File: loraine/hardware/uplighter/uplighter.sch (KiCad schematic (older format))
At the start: 10 parts, among them K1 CONN_3, K2 CONN_3, K3 CONN_3, U1 TL4242, U2 TL4242, U3 TL4242

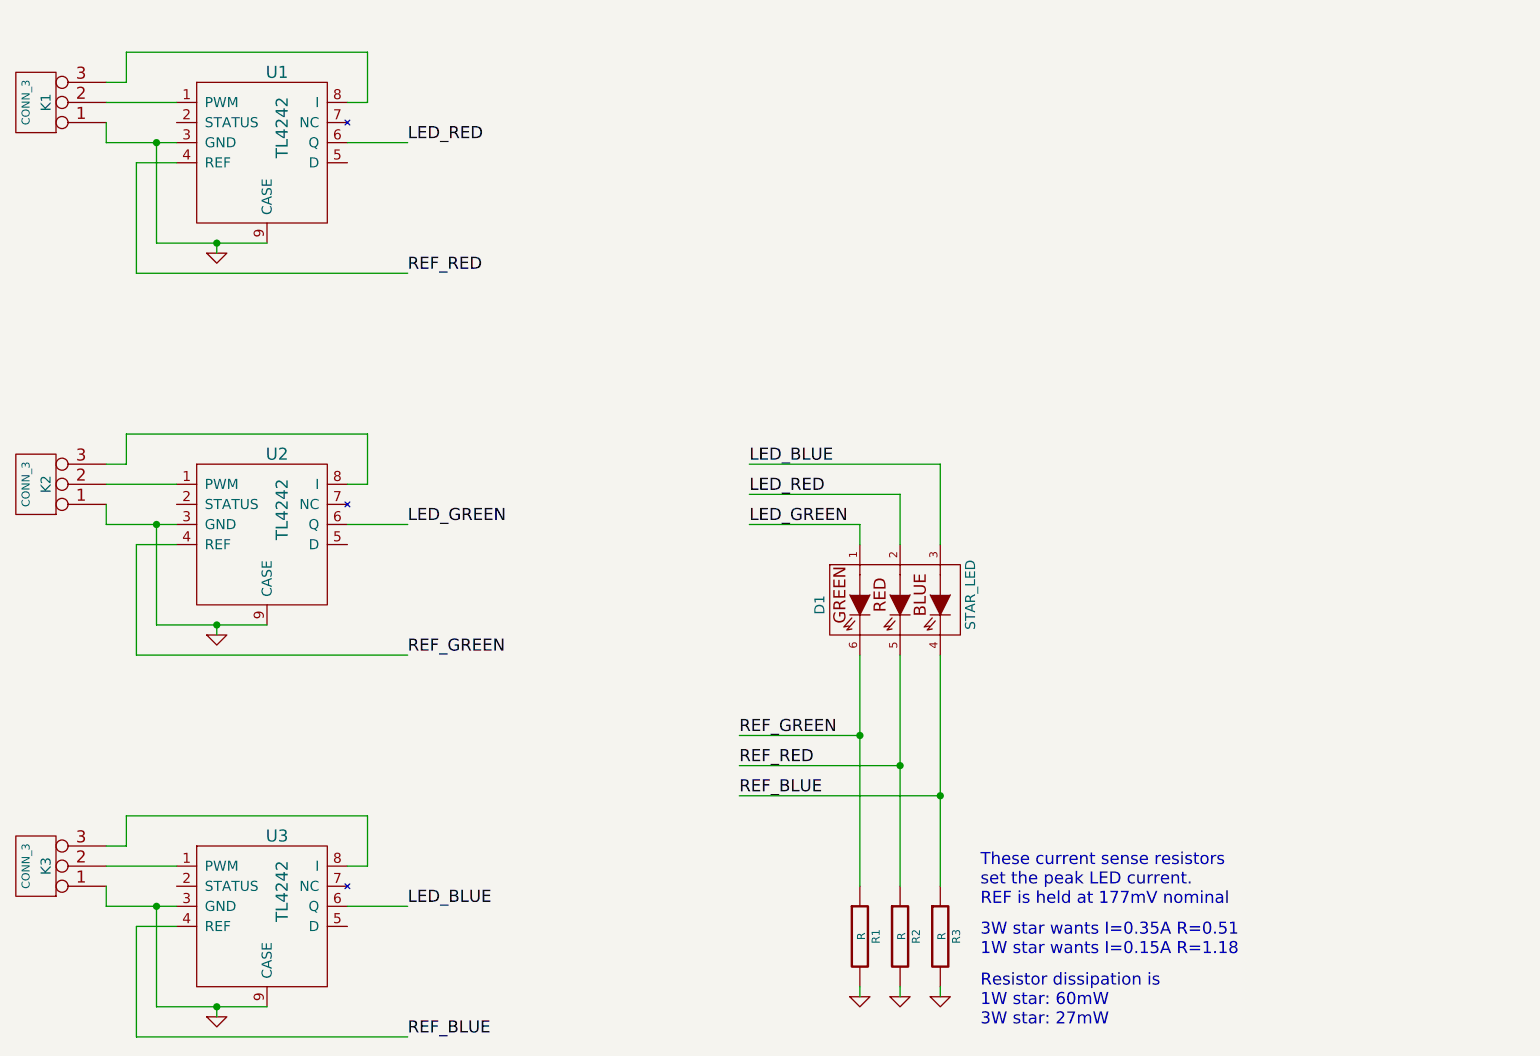
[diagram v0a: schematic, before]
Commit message: Proposed output driver for node h/w
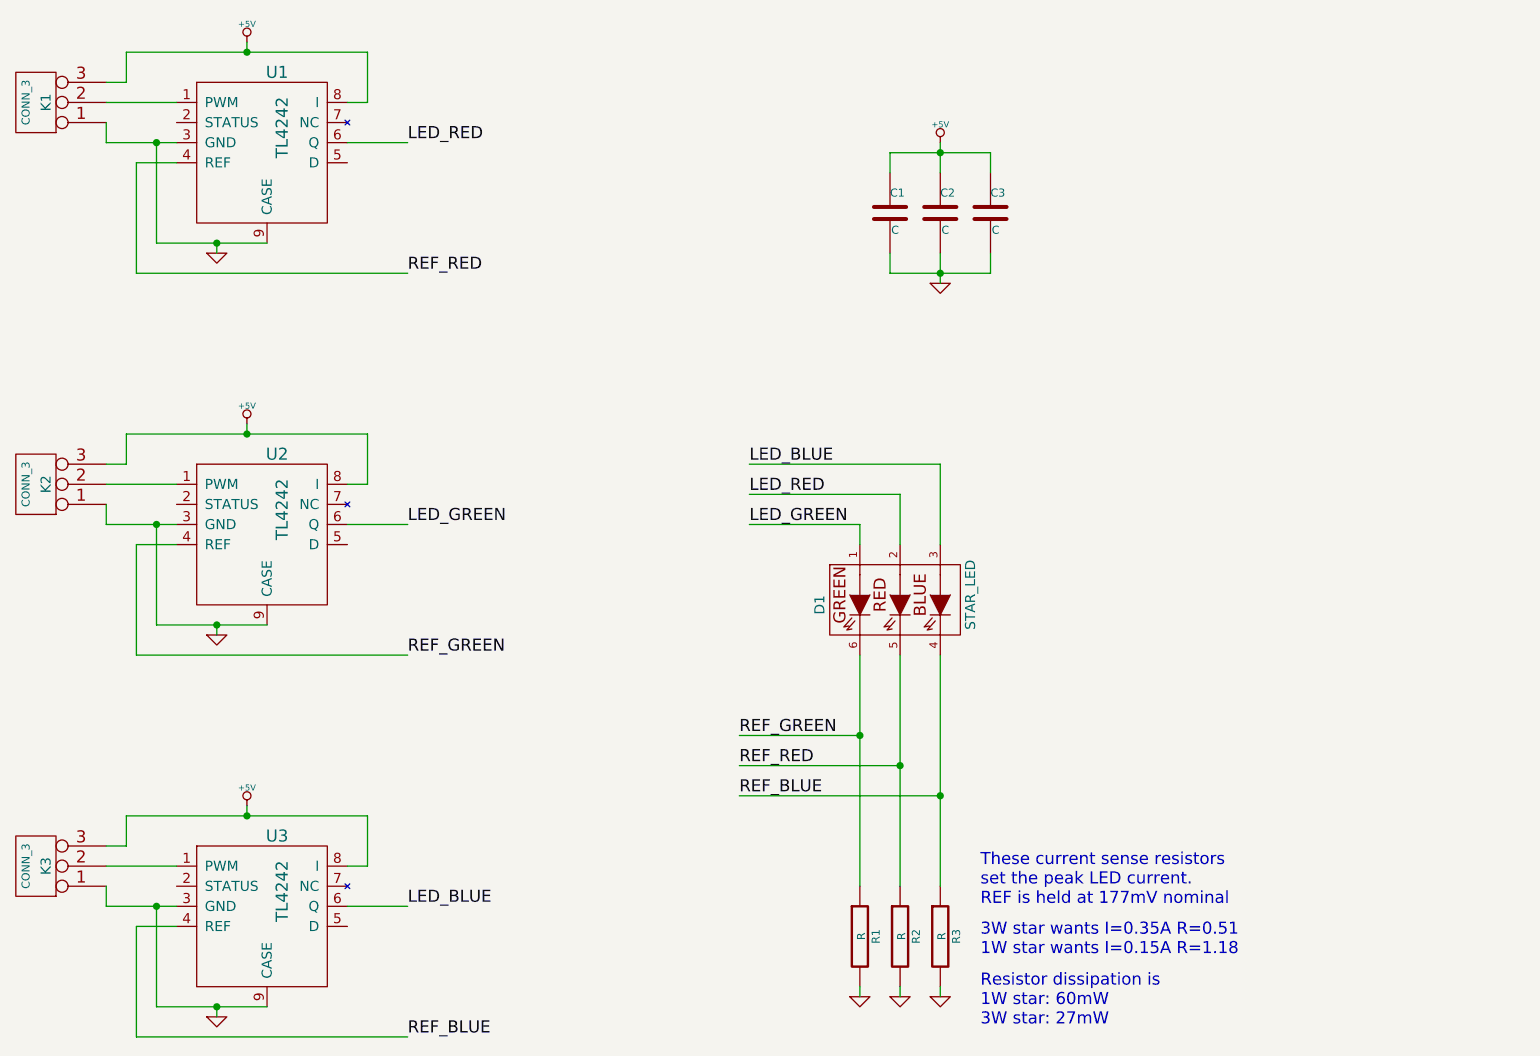
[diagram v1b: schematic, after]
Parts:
- added C1, C2, C3: C, symbol C
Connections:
- net GND: now also C1.2, C2.2, C3.2
- net +5V: now reaches K1.3 (P3), U1.8 (I)
- net +5V: now also K2.3 (P3), K3.3 (P3), U2.8 (I), U3.8 (I), C1.1, C2.1, C3.1
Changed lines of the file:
@@
 	1    0    0    -1
 $EndComp
-Wire Wire Line
-	3150 1650 3450 1650
-Wire Wire Line
-	1950 1650 2300 1650
-Wire Wire Line
-	2200 2150 2750 2150
-Wire Wire Line
-	2200 1650 2200 2150
-Wire Wire Line
-	2300 1750 2100 1750
-Wire Wire Line
-	1950 1450 2300 1450
-Wire Wire Line
-	1950 1350 2050 1350
-Wire Wire Line
-	2050 1350 2050 1200
-Wire Wire Line
-	2050 1200 3250 1200
-Wire Wire Line
-	3250 1200 3250 1450
-Wire Wire Line
-	3250 1450 3150 1450
-Wire Wire Line
-	1950 1550 1950 1650
-Connection ~ 2200 1650
-Wire Wire Line
-	2100 1750 2100 2300
-Wire Wire Line
-	2100 2300 3450 2300
-Wire Wire Line
-	3150 3550 3450 3550
-Wire Wire Line
-	1950 3550 2300 3550
-Wire Wire Line
-	2200 4050 2750 4050
-Wire Wire Line
-	2200 3550 2200 4050
-Wire Wire Line
-	2300 3650 2100 3650
-Wire Wire Line
-	1950 3350 2300 3350
-Wire Wire Line
-	1950 3250 2050 3250
-Wire Wire Line
-	2050 3250 2050 3100
-Wire Wire Line
-	2050 3100 3250 3100
-Wire Wire Line
-	3250 3100 3250 3350
-Wire Wire Line
-	3250 3350 3150 3350
-Wire Wire Line
-	1950 3450 1950 3550
-Connection ~ 2200 3550
-Wire Wire Line
-	2100 3650 2100 4200
-Wire Wire Line
-	2100 4200 3450 4200
-Wire Wire Line
-	3150 5450 3450 5450
-Wire Wire Line
-	1950 5450 2300 5450
-Wire Wire Line
-	2200 5950 2750 5950
-Wire Wire Line
-	2200 5450 2200 5950
-Wire Wire Line
-	2300 5550 2100 5550
-Wire Wire Line
-	1950 5250 2300 5250
-Wire Wire Line
-	1950 5150 2050 5150
-Wire Wire Line
-	2050 5150 2050 5000
-Wire Wire Line
-	2050 5000 3250 5000
-Wire Wire Line
-	3250 5000 3250 5250
-Wire Wire Line
-	3250 5250 3150 5250
-Wire Wire Line
-	1950 5350 1950 5450
-Connection ~ 2200 5450
-Wire Wire Line
-	2100 5550 2100 6100
-Wire Wire Line
-	2100 6100 3450 6100
-Wire Wire Line
-	5700 4200 5700 5350
-Wire Wire Line
-	5900 4200 5900 5350
-Wire Wire Line
-	6100 4200 6100 5350
-Wire Wire Line
-	6100 5850 6100 5900
-Wire Wire Line
-	5900 5900 5900 5850
-Wire Wire Line
-	5700 5850 5700 5900
-Wire Wire Line
-	2500 2200 2500 2150
-Connection ~ 2500 2150
 $Comp
 L GND #PWR05
@@
 	1    0    0    -1
 $EndComp
-Wire Wire Line
-	2500 4100 2500 4050
-Connection ~ 2500 4050
 $Comp
 L GND #PWR06
@@
 	1    0    0    -1
 $EndComp
-Wire Wire Line
-	2500 6000 2500 5950
-Connection ~ 2500 5950
 Text Label 5150 3550 0    60   ~ 0
 LED_GREEN
@@
 Text Label 5150 3250 0    60   ~ 0
 LED_BLUE
-Wire Wire Line
-	5150 3250 6100 3250
-Wire Wire Line
-	6100 3250 6100 3650
-Wire Wire Line
-	5150 3400 5900 3400
-Wire Wire Line
-	5900 3400 5900 3650
-Wire Wire Line
-	5150 3550 5700 3550
-Wire Wire Line
-	5700 3550 5700 3650
 Text Label 5100 4600 0    60   ~ 0
 REF_GREEN
@@
 Text Label 5100 4750 0    60   ~ 0
 REF_RED
+$Comp
+L +5V #PWR07
+U 1 1 537A665B
+P 2650 1150
+F 0 "#PWR07" H 2650 1240 20  0001 C CNN
+F 1 "+5V" H 2650 1240 30  0000 C CNN
+F 2 "" H 2650 1150 60  0000 C CNN
+F 3 "" H 2650 1150 60  0000 C CNN
+	1    2650 1150
+	1    0    0    -1
+$EndComp
+$Comp
+L +5V #PWR08
+U 1 1 537A6711
+P 2650 3050
+F 0 "#PWR08" H 2650 3140 20  0001 C CNN
+F 1 "+5V" H 2650 3140 30  0000 C CNN
+F 2 "" H 2650 3050 60  0000 C CNN
+F 3 "" H 2650 3050 60  0000 C CNN
+	1    2650 3050
+	1    0    0    -1
+$EndComp
+$Comp
+L +5V #PWR09
+U 1 1 537A67B5
+P 2650 4950
+F 0 "#PWR09" H 2650 5040 20  0001 C CNN
+F 1 "+5V" H 2650 5040 30  0000 C CNN
+F 2 "" H 2650 4950 60  0000 C CNN
+F 3 "" H 2650 4950 60  0000 C CNN
+	1    2650 4950
+	1    0    0    -1
+$EndComp
+$Comp
+L +5V #PWR010
+U 1 1 537A6897
+P 6100 1650
+F 0 "#PWR010" H 6100 1740 20  0001 C CNN
+F 1 "+5V" H 6100 1740 30  0000 C CNN
+F 2 "" H 6100 1650 60  0000 C CNN
+F 3 "" H 6100 1650 60  0000 C CNN
+	1    6100 1650
+	1    0    0    -1
+$EndComp
+$Comp
+L C C1
+U 1 1 537A69DC
+P 5850 2000
+F 0 "C1" H 5850 2100 40  0000 L CNN
+F 1 "C" H 5856 1915 40  0000 L CNN
+F 2 "" H 5888 1850 30  0000 C CNN
+F 3 "" H 5850 2000 60  0000 C CNN
+	1    5850 2000
+	1    0    0    -1
+$EndComp
+$Comp
+L C C2
+U 1 1 537A6A0C
+P 6100 2000
+F 0 "C2" H 6100 2100 40  0000 L CNN
+F 1 "C" H 6106 1915 40  0000 L CNN
+F 2 "" H 6138 1850 30  0000 C CNN
+F 3 "" H 6100 2000 60  0000 C CNN
+	1    6100 2000
+	1    0    0    -1
+$EndComp
+$Comp
+L C C3
+U 1 1 537A6A35
+P 6350 2000
+F 0 "C3" H 6350 2100 40  0000 L CNN
+F 1 "C" H 6356 1915 40  0000 L CNN
+F 2 "" H 6388 1850 30  0000 C CNN
+F 3 "" H 6350 2000 60  0000 C CNN
+	1    6350 2000
+	1    0    0    -1
+$EndComp
+Wire Wire Line
+	3150 1650 3450 1650
+Wire Wire Line
+	1950 1650 2300 1650
+Wire Wire Line
+	2200 2150 2750 2150
+Wire Wire Line
+	2200 1650 2200 2150
+Wire Wire Line
+	2300 1750 2100 1750
+Wire Wire Line
+	1950 1450 2300 1450
+Wire Wire Line
+	1950 1350 2050 1350
+Wire Wire Line
+	2050 1350 2050 1200
+Wire Wire Line
+	2050 1200 3250 1200
+Wire Wire Line
+	3250 1200 3250 1450
+Wire Wire Line
+	3250 1450 3150 1450
+Wire Wire Line
+	1950 1550 1950 1650
+Connection ~ 2200 1650
+Wire Wire Line
+	2100 1750 2100 2300
+Wire Wire Line
+	2100 2300 3450 2300
+Wire Wire Line
+	3150 3550 3450 3550
+Wire Wire Line
+	1950 3550 2300 3550
+Wire Wire Line
+	2200 4050 2750 4050
+Wire Wire Line
+	2200 3550 2200 4050
+Wire Wire Line
+	2300 3650 2100 3650
+Wire Wire Line
+	1950 3350 2300 3350
+Wire Wire Line
+	1950 3250 2050 3250
+Wire Wire Line
+	2050 3250 2050 3100
+Wire Wire Line
+	2050 3100 3250 3100
+Wire Wire Line
+	3250 3100 3250 3350
+Wire Wire Line
+	3250 3350 3150 3350
+Wire Wire Line
+	1950 3450 1950 3550
+Connection ~ 2200 3550
+Wire Wire Line
+	2100 3650 2100 4200
+Wire Wire Line
+	2100 4200 3450 4200
+Wire Wire Line
+	3150 5450 3450 5450
+Wire Wire Line
+	1950 5450 2300 5450
+Wire Wire Line
+	2200 5950 2750 5950
+Wire Wire Line
+	2200 5450 2200 5950
+Wire Wire Line
+	2300 5550 2100 5550
+Wire Wire Line
+	1950 5250 2300 5250
+Wire Wire Line
+	1950 5150 2050 5150
+Wire Wire Line
+	2050 5150 2050 5000
+Wire Wire Line
+	2050 5000 3250 5000
+Wire Wire Line
+	3250 5000 3250 5250
+Wire Wire Line
+	3250 5250 3150 5250
+Wire Wire Line
+	1950 5350 1950 5450
+Connection ~ 2200 5450
+Wire Wire Line
+	2100 5550 2100 6100
+Wire Wire Line
+	2100 6100 3450 6100
+Wire Wire Line
+	5700 4200 5700 5350
+Wire Wire Line
+	5900 4200 5900 5350
+Wire Wire Line
+	6100 4200 6100 5350
+Wire Wire Line
+	6100 5850 6100 5900
+Wire Wire Line
+	5900 5900 5900 5850
+Wire Wire Line
+	5700 5850 5700 5900
+Wire Wire Line
+	2500 2200 2500 2150
+Connection ~ 2500 2150
+Wire Wire Line
+	2500 4100 2500 4050
+Connection ~ 2500 4050
+Wire Wire Line
+	2500 6000 2500 5950
+Connection ~ 2500 5950
+Wire Wire Line
+	5150 3250 6100 3250
+Wire Wire Line
+	6100 3250 6100 3650
+Wire Wire Line
+	5150 3400 5900 3400
+Wire Wire Line
+	5900 3400 5900 3650
+Wire Wire Line
+	5150 3550 5700 3550
+Wire Wire Line
+	5700 3550 5700 3650
 Wire Wire Line
 	5100 4600 5700 4600
@@
 	5100 4900 6100 4900
 Connection ~ 6100 4900
+Wire Wire Line
+	2650 1150 2650 1200
+Connection ~ 2650 1200
+Wire Wire Line
+	2650 3050 2650 3100
+Connection ~ 2650 3100
+Wire Wire Line
+	2650 4950 2650 5000
+Connection ~ 2650 5000
+Wire Wire Line
+	5850 1800 5850 1700
+Wire Wire Line
+	5850 1700 6350 1700
+Wire Wire Line
+	6350 1700 6350 1800
+Wire Wire Line
+	6100 1650 6100 1800
+Connection ~ 6100 1700
+$Comp
+L GND #PWR011
+U 1 1 537A6CCB
+P 6100 2350
+F 0 "#PWR011" H 6100 2350 30  0001 C CNN
+F 1 "GND" H 6100 2280 30  0001 C CNN
+F 2 "" H 6100 2350 60  0000 C CNN
+F 3 "" H 6100 2350 60  0000 C CNN
+	1    6100 2350
+	1    0    0    -1
+$EndComp
+Wire Wire Line
+	6100 2200 6100 2350
+Wire Wire Line
+	5850 2300 6350 2300
+Wire Wire Line
+	5850 2300 5850 2200
+Connection ~ 6100 2300
+Wire Wire Line
+	6350 2300 6350 2200
 $EndSCHEMATC
